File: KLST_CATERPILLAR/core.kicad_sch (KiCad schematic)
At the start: 34 parts, among them SW1 BUTTON_RESET, SW2 BUTTON_BOOT_FLASH, U2 STM32H723ZGTx, Y1 16MHz

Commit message: reduced modules
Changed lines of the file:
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@@
+		)
+	)
+	(text_box "@TODO(@maybe get rid of buttons)"
+		(exclude_from_sim no)
+		(at 187.96 186.69 0)
+		(size 201.295 14.605)
+		(stroke
+			(width -0.0001)
+			(type default)
+		)
+		(fill
+			(type color)
+			(color 255 0 0 1)
+		)
+		(effects
+			(font
+				(size 5.08 5.08)
+			)
+			(justify left top)
 		)
 	)
@@
 			)
 			(justify left top)
+		)
+	)
+	(text_box "@TODO(maybe PIN out fot GPIOs THT:C79866 or SMD:C601974/C2829932)"
+		(exclude_from_sim no)
+		(at 187.96 207.645 0)
+		(size 202.565 34.925)
+		(stroke
+			(width -0.0001)
+			(type default)
+		)
+		(fill
+			(type color)
+			(color 255 0 0 1)
+		)
+		(effects
+			(font
+				(size 5.08 5.08)
+			)
+			(justify left top)

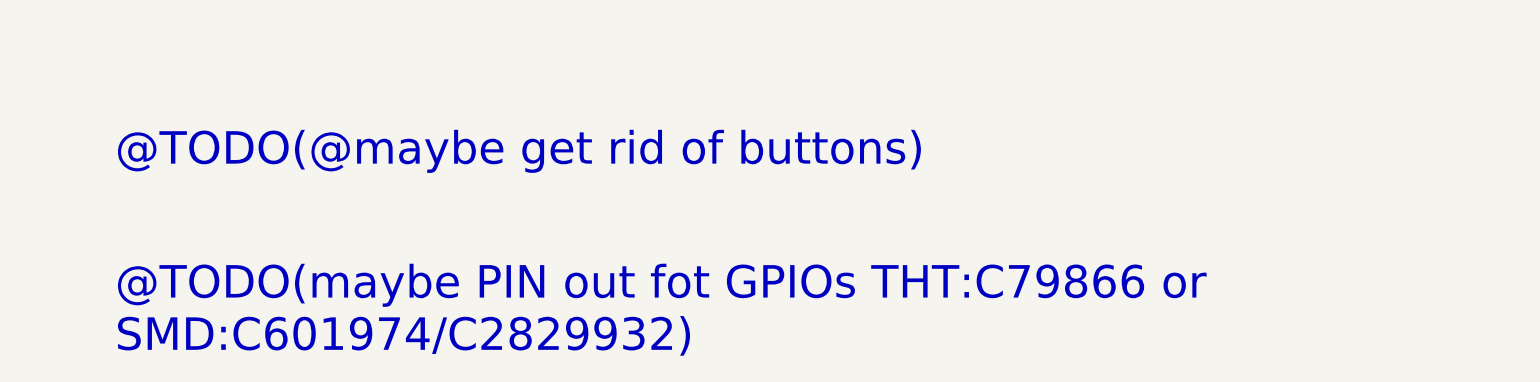
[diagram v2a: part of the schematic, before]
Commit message: added test points, replaced unavailable components
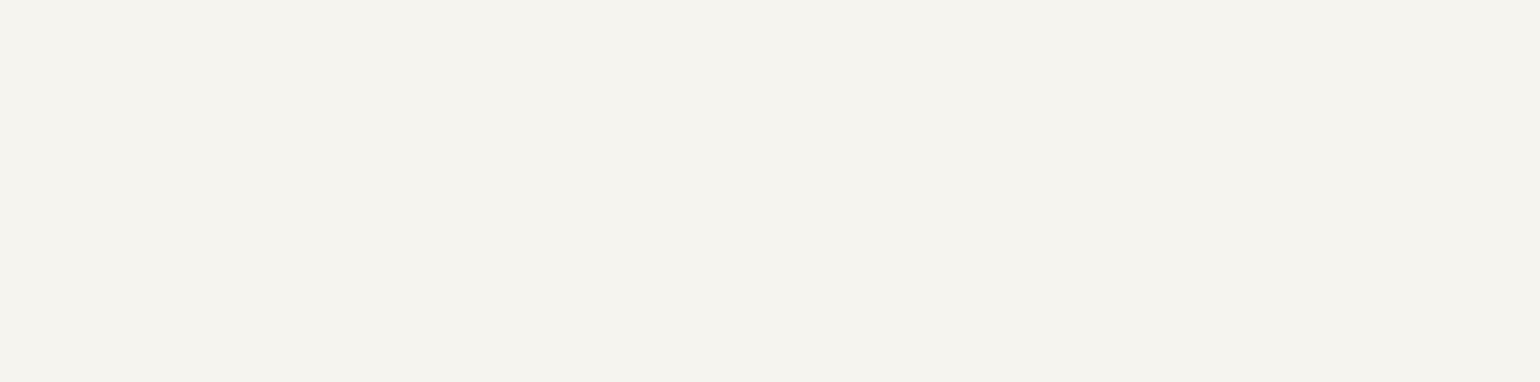
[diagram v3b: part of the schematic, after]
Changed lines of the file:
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@@
-		)
-	)
-	(text_box "@TODO(@maybe get rid of buttons)"
-		(exclude_from_sim no)
-		(at 187.96 186.69 0)
-		(size 201.295 14.605)
-		(stroke
-			(width -0.0001)
-			(type default)
-		)
-		(fill
-			(type color)
-			(color 255 0 0 1)
-		)
-		(effects
-			(font
-				(size 5.08 5.08)
-			)
-			(justify left top)
 		)
 	)
@@
 			)
 			(justify left top)
-		)
-	)
-	(text_box "@TODO(maybe PIN out fot GPIOs THT:C79866 or SMD:C601974/C2829932)"
-		(exclude_from_sim no)
-		(at 187.96 207.645 0)
-		(size 202.565 34.925)
-		(stroke
-			(width -0.0001)
-			(type default)
-		)
-		(fill
-			(type color)
-			(color 255 0 0 1)
-		)
-		(effects
-			(font
-				(size 5.08 5.08)
-			)
-			(justify left top)
